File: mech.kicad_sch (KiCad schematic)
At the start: 17 parts

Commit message: date update
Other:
- title: M17 Remote Radio Unit - RF board -> Remote Radio Unit - RF board
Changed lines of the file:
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@@
   (paper "A3")
   (title_block
-    (title "M17 Remote Radio Unit - RF board")
-    (date "28-10-2023")
+    (title "Remote Radio Unit - RF board")
+    (date "30-10-2023")
     (rev "A")
     (company "M17 Project")

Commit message: MPN/PN update
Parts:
- FID1, FID2, FID3, H1, H10, H11, H12, H13, H14, H2, H3, H4, H5, H6, H7, H8, H9: MPN (none) -> -; PN (none) -> -
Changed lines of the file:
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@@
+      (effects (font (size 1.27 1.27)) hide)
+    )
+    (property "MPN" "-" (at 137.16 102.87 0)
+      (effects (font (size 1.27 1.27)) hide)
+    )
+    (property "PN" "-" (at 137.16 102.87 0)
       (effects (font (size 1.27 1.27)) hide)
     )
@@
       (effects (font (size 1.27 1.27)) hide)
     )
+    (property "MPN" "-" (at 247.65 106.68 0)
+      (effects (font (size 1.27 1.27)) hide)
+    )
+    (property "PN" "-" (at 247.65 106.68 0)
+      (effects (font (size 1.27 1.27)) hide)
+    )
     (pin "1")
     (instances
@@
       (effects (font (size 1.27 1.27)) hide)
     )
+    (property "MPN" "-" (at 259.08 120.65 0)
+      (effects (font (size 1.27 1.27)) hide)
+    )
+    (property "PN" "-" (at 259.08 120.65 0)
+      (effects (font (size 1.27 1.27)) hide)
+    )
     (pin "1")
     (instances
@@
       (effects (font (size 1.27 1.27)) hide)
     )
+    (property "MPN" "-" (at 162.56 102.87 0)
+      (effects (font (size 1.27 1.27)) hide)
+    )
+    (property "PN" "-" (at 162.56 102.87 0)
+      (effects (font (size 1.27 1.27)) hide)
+    )
     (instances
       (project "m17-rru-rf"
@@
       (effects (font (size 1.27 1.27)) hide)
     )
+    (property "MPN" "-" (at 247.65 120.65 0)
+      (effects (font (size 1.27 1.27)) hide)
+    )
+    (property "PN" "-" (at 247.65 120.65 0)
+      (effects (font (size 1.27 1.27)) hide)
+    )
     (pin "1")
     (instances
@@
       (effects (font (size 1.27 1.27)) hide)
     )
+    (property "MPN" "-" (at 270.51 106.68 0)
+      (effects (font (size 1.27 1.27)) hide)
+    )
+    (property "PN" "-" (at 270.51 106.68 0)
+      (effects (font (size 1.27 1.27)) hide)
+    )
     (pin "1")
     (instances
@@
     )
     (property "Datasheet" "~" (at 270.51 78.74 0)
+      (effects (font (size 1.27 1.27)) hide)
+    )
+    (property "MPN" "-" (at 270.51 78.74 0)
+      (effects (font (size 1.27 1.27)) hide)
+    )
+    (property "PN" "-" (at 270.51 78.74 0)
       (effects (font (size 1.27 1.27)) hide)
     )
@@
       (effects (font (size 1.27 1.27)) hide)
     )
+    (property "MPN" "-" (at 247.65 78.74 0)
+      (effects (font (size 1.27 1.27)) hide)
+    )
+    (property "PN" "-" (at 247.65 78.74 0)
+      (effects (font (size 1.27 1.27)) hide)
+    )
     (pin "1")
     (instances
@@
       (effects (font (size 1.27 1.27)) hide)
     )
+    (property "MPN" "-" (at 281.94 106.68 0)
+      (effects (font (size 1.27 1.27)) hide)
+    )
+    (property "PN" "-" (at 281.94 106.68 0)
+      (effects (font (size 1.27 1.27)) hide)
+    )
     (pin "1")
     (instances
@@
       (effects (font (size 1.27 1.27)) hide)
     )
+    (property "MPN" "-" (at 281.94 92.71 0)
+      (effects (font (size 1.27 1.27)) hide)
+    )
+    (property "PN" "-" (at 281.94 92.71 0)
+      (effects (font (size 1.27 1.27)) hide)
+    )
     (pin "1")
     (instances
@@
       (effects (font (size 1.27 1.27)) hide)
     )
+    (property "MPN" "-" (at 270.51 92.71 0)
+      (effects (font (size 1.27 1.27)) hide)
+    )
+    (property "PN" "-" (at 270.51 92.71 0)
+      (effects (font (size 1.27 1.27)) hide)
+    )
     (pin "1")
     (instances
@@
       (effects (font (size 1.27 1.27)) hide)
     )
+    (property "MPN" "-" (at 259.08 92.71 0)
+      (effects (font (size 1.27 1.27)) hide)
+    )
+    (property "PN" "-" (at 259.08 92.71 0)
+      (effects (font (size 1.27 1.27)) hide)
+    )
     (pin "1")
     (instances
@@
       (effects (font (size 1.27 1.27)) hide)
     )
+    (property "MPN" "-" (at 281.94 78.74 0)
+      (effects (font (size 1.27 1.27)) hide)
+    )
+    (property "PN" "-" (at 281.94 78.74 0)
+      (effects (font (size 1.27 1.27)) hide)
+    )
     (pin "1")
     (instances
@@
       (effects (font (size 1.27 1.27)) hide)
     )
+    (property "MPN" "-" (at 259.08 106.68 0)
+      (effects (font (size 1.27 1.27)) hide)
+    )
+    (property "PN" "-" (at 259.08 106.68 0)
+      (effects (font (size 1.27 1.27)) hide)
+    )
     (pin "1")
     (instances
@@
       (effects (font (size 1.27 1.27)) hide)
     )
+    (property "MPN" "-" (at 247.65 92.71 0)
+      (effects (font (size 1.27 1.27)) hide)
+    )
+    (property "PN" "-" (at 247.65 92.71 0)
+      (effects (font (size 1.27 1.27)) hide)
+    )
     (pin "1")
     (instances
@@
       (effects (font (size 1.27 1.27)) hide)
     )
+    (property "MPN" "-" (at 149.86 102.87 0)
+      (effects (font (size 1.27 1.27)) hide)
+    )
+    (property "PN" "-" (at 149.86 102.87 0)
+      (effects (font (size 1.27 1.27)) hide)
+    )
     (instances
       (project "m17-rru-rf"
@@
       (effects (font (size 1.27 1.27)) hide)
     )
+    (property "MPN" "-" (at 259.08 78.74 0)
+      (effects (font (size 1.27 1.27)) hide)
+    )
+    (property "PN" "-" (at 259.08 78.74 0)
+      (effects (font (size 1.27 1.27)) hide)
+    )

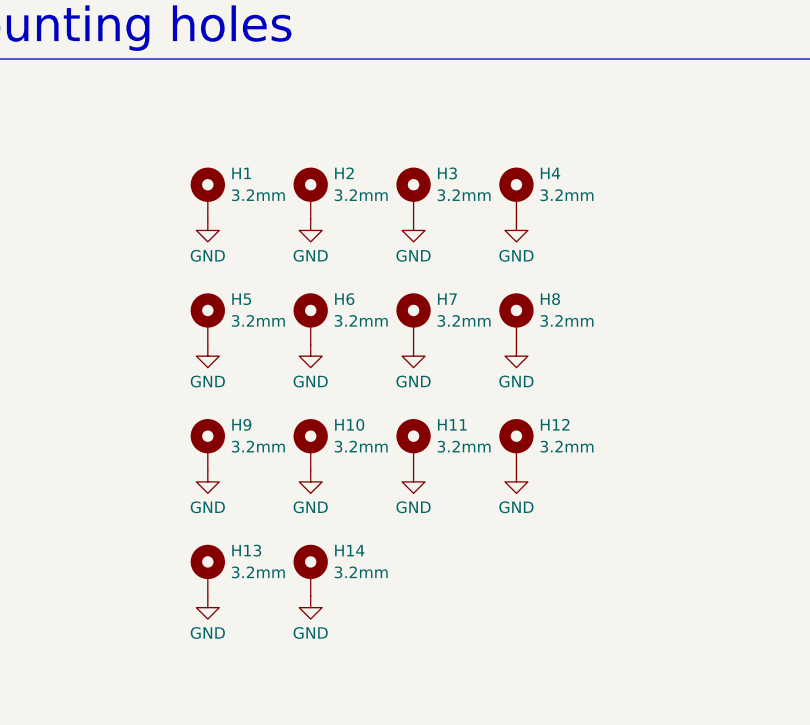
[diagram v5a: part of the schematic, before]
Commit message: WIP rev B
- replaced R44-R46 with 22k
- exposed BOOT0 at the DA15 connector
- added a testpoint at DAC OUT2
- added a buffer to the 40MHz reference oscillator
- removed C2
- bypassed R5 with a 100nF capacitor
- changed D5's voltage to 5.1V
- routed TX_SAMP_CLK
- changed temperature sensor's supply voltage to 5V
- added a series of 100p, 1n and 10n capacitors at PA_VGG
- reduced N-connector cutouts to 2.5mm
- improved RF output track a little
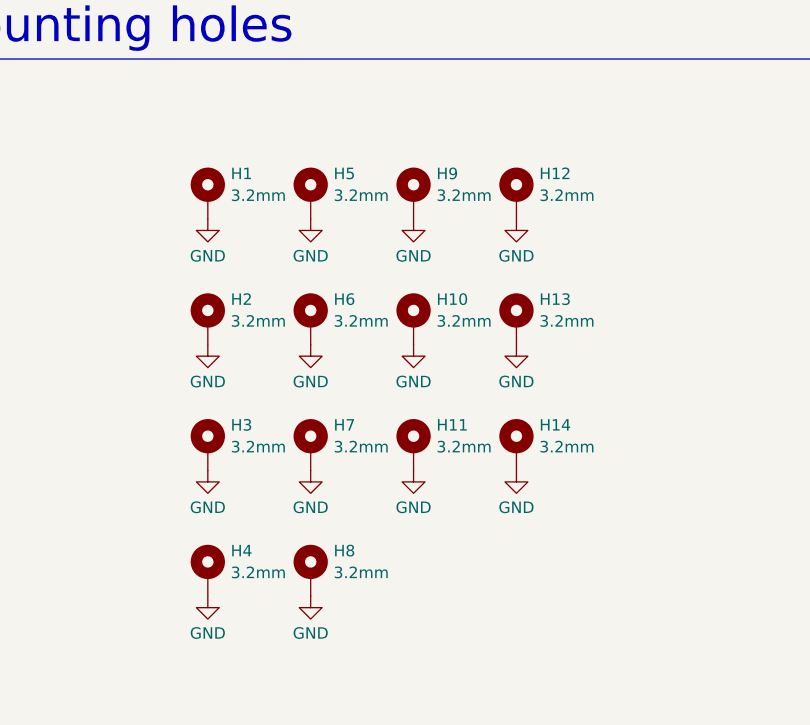
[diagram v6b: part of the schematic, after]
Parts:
- renumbered H7 to H10, H4 to H12, H8 to H13, H12 to H14, H5 to H2, H9 to H3, H13 to H4, H2 to H5, H10 to H7, H14 to H8, H3 to H9
